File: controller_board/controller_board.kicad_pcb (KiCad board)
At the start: 2 copper layers, 91.6 x 73.5 mm, 135 parts, among them CN7 DS1023-2x19S21, CN9 DS1023-2x19S21, IC1 LD1117-3.3V-SOT223, J1 DG141R-02 (RS485), J5 DS1027-2B и PinHeader_2x01_P2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, J6 PLL-10 (Prog), Q1 DTC114ECA (SOT-23), Q2 DTC114ECA (SOT-23), U1 ADM3485EARZ-REEL (SOIC-8), U2 pia141M30 (SOIC-16)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

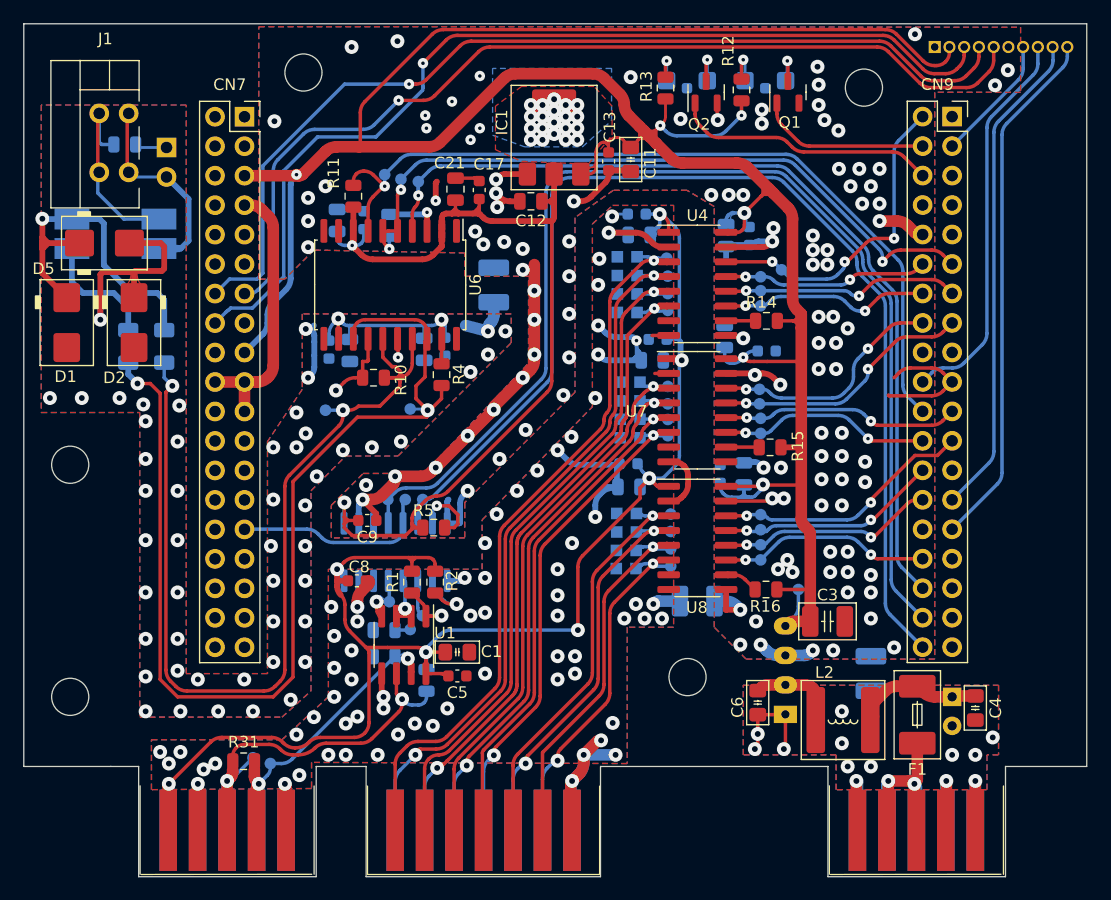
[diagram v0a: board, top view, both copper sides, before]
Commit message: digit_in  убраны ловушки
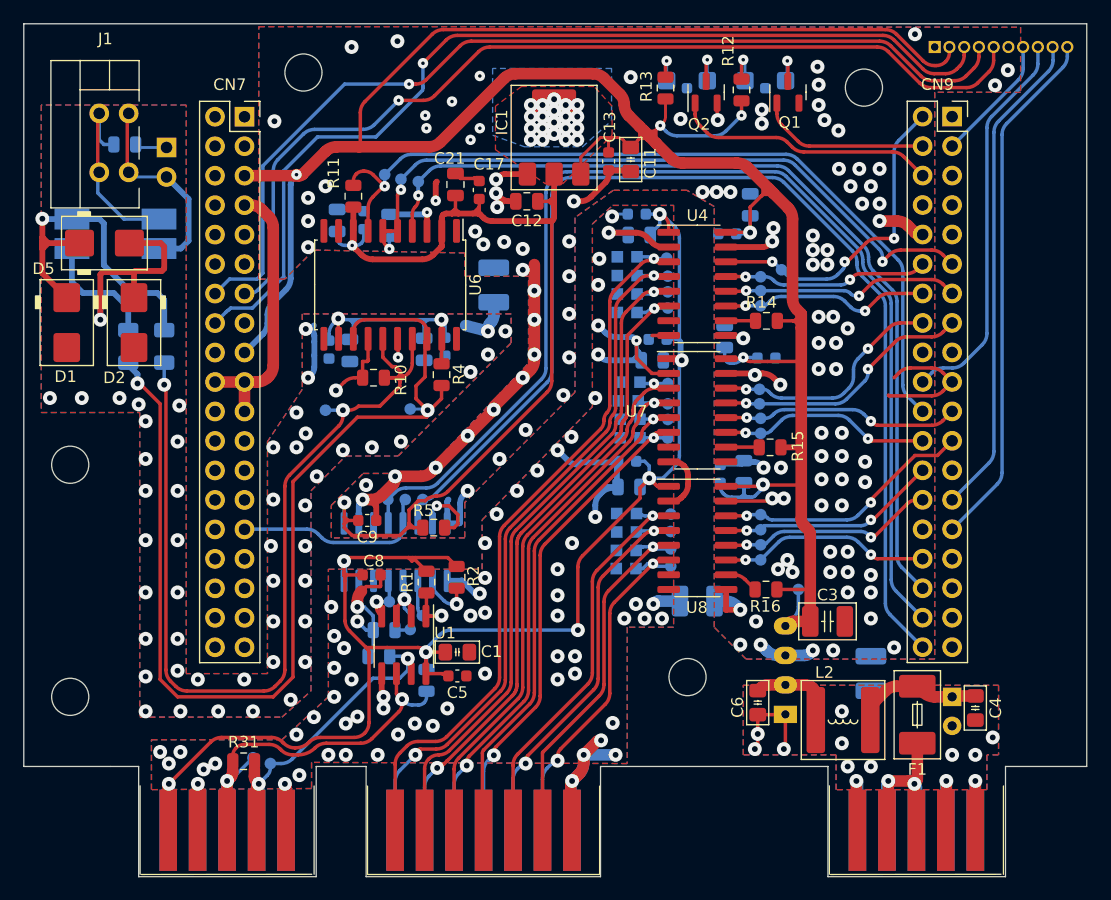
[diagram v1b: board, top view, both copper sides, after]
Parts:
- moved C23 3.37 mm to (152.6, 51.6), turned to -90 degrees
- moved C24 1.91 mm to (150.6, 54.1), turned to 180 degrees
- moved R2 1.90 mm to (127.3, 83.7)
- moved C8 1.36 mm to (120.0, 83.5)
- moved R1 1.25 mm to (124.7, 84.1)
- moved C25 0.60 mm to (154.0, 64.8)
- moved R6 0.45 mm to (120.6, 90.5)
- moved C21 0.40 mm to (127.2, 49.9)
- moved C12 0.35 mm to (133.3, 51.3)
- moved TP17 0.25 mm to (145.5, 67.0)
- moved C34 0.24 mm to (142.0, 73.7)
- moved TP16 0.20 mm to (145.5, 60.5)
- moved TP20 0.20 mm to (145.5, 71.7)
- moved C28 0.19 mm to (152.1, 74.6)
- moved R25 0.15 mm to (142.1, 68.5)
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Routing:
- net GND1: track 86.3 -> 100.0 mm
- net GNDD: track 137.1 -> 132.8 mm
- net /+3.3VRS485: track 141.7 -> 145.9 mm
- net +5V: track 247.6 -> 250.4 mm
- net Net-(RS1-Pin_4): track 28.4 -> 30.6 mm
- net Net-(U6-Visoin): track 22.9 -> 24.9 mm
- net /USART1_RTS: track 61.3 -> 62.7 mm
- net Net-(U1-DE): track 7.84 -> 9.20 mm
- net Net-(U2-VE2): track 5.43 -> 4.60 mm
- net +3V3: track 83.6 -> 84.2 mm
- net Net-(U6-A): track 94.1 -> 93.6 mm

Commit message: controller метализированные отверстия
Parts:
- H3, H4, H5: footprint MountingHole:MountingHole_3.2mm_M3 -> MountingHole:MountingHole_3.2mm_M3_DIN965_Pad
- moved C27 4.74 mm to (154.4, 76.6), turned to 0 degrees
- moved C28 2.31 mm to (154.3, 74.8), turned to 180 degrees
- moved C34 0.40 mm to (142.0, 74.1)
- moved C8 0.20 mm to (119.8, 83.5)
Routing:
- net GND1: track 100.0 -> 93.5 mm, vias 67 -> 65
- net +5V: track 250.4 -> 244.2 mm
- net Net-(RS2-Pin_2): track 22.6 -> 28.5 mm
- net GND2: track 18.6 -> 13.6 mm
- net GNDD: track 132.8 -> 128.2 mm, vias 115 -> 113
- net /+3.3VRS485: track 145.9 -> 143.3 mm
- net GNDA: track 34.0 -> 31.6 mm, vias 13 -> 10
- net +24V: track 11.1 -> 12.6 mm
- net Net-(RS1-Pin_4): track 30.6 -> 31.4 mm
- net Net-(U6-B): track 83.6 -> 82.8 mm

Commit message: controller тестовые площадки
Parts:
- added G1: TestPoint, PCM_4ms_TestPoint:TestPoint_D1, B.Cu at (132.9, 95.6)
- added GA1: TestPoint, PCM_4ms_TestPoint:TestPoint_D1, B.Cu at (164.0, 96.9)
- added GD1: TestPoint, PCM_4ms_TestPoint:TestPoint_D1, B.Cu at (128.3, 51.8)
- moved C22 0.52 mm to (118.8, 52.8)
- moved C31 0.29 mm to (144.4, 65.0)
- moved C32 0.18 mm to (144.8, 63.2)
- moved R25 0.15 mm to (142.2, 68.5)
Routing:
- net GND1: track 93.5 -> 76.7 mm
- net GNDA: track 31.6 -> 37.7 mm
- net GNDD: track 128.2 -> 124.0 mm
- net /+3.3VRS485: track 143.3 -> 144.4 mm

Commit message: controller кислотные ловушки
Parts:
- moved C17 2.97 mm to (126.3, 50.0)
- moved C21 0.90 mm to (128.1, 49.9)
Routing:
- net GNDD: track 124.0 -> 120.7 mm
- net Net-(U6-Visoin): track 24.9 -> 23.0 mm
- net +5V: track 244.2 -> 244.8 mm
- net GND1: track 76.7 -> 76.8 mm, vias 65 -> 64

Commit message: controller кислотные ловушки1
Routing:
- net GNDD: track 120.7 -> 113.6 mm
- net GND1: track 76.8 -> 72.5 mm
- net /+3.3VRS485: track 144.4 -> 143.3 mm
